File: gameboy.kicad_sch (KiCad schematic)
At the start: 17 parts, among them J1 FPC-05F-12PH20, J2 Conn_ST_STDC14, J3 Conn_01x02, U1 TP4056-42-ESOP8, U2 STM32F722RETx, Y1 26MHz

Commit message: start with power management
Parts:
- removed C3: C, symbol Device:C
- removed C4: 10uF, symbol Device:C
- removed D1, D2: LED, symbol Device:LED
- removed J3: Conn_01x02, Connector_JST:JST_PH_B2B-PH-K_1x02_P2.00mm_Vertical, symbol Connector_Generic:Conn_01x02
- removed R2: 2.2k, symbol Device:R
- removed R3, R4: 1k, symbol Device:R
- removed U1: TP4056-42-ESOP8, Package_SO:SOIC-8-1EP_3.9x4.9mm_P1.27mm_EP2.41x3.3mm_ThermalVias, symbol Battery_Management:TP4056-42-ESOP8
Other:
- added sheet Power (power.kicad_sch)
- note removed: "0.5C = half the battery capacity per hour 1000mAh => 500mA = I_{BAT} charge current R_{prog} = 1100 / I_{BAT} = 2.2k"
- note removed: "523450 LiPo 3.7V, 1000mAh"

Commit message: led driver backlight, not finished
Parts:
- added C8, C9: 1uF, Capacitor_SMD:C_0603_1608Metric, symbol Device:C
- added D5: D, symbol Device:D_Schottky
- added L2: 22uH, Inductor_SMD:L_KOHERelec_MDA7030, symbol Device:L
- added R11: 1.25R, Resistor_SMD:R_0603_1608Metric, symbol Device:R
- added U3: AP5724WG-7, SOT26_DIO:SOT26_DIO, symbol SOT26_DIO:AP5724WG-7
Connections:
- net GND: now also C8.2, C9.2, R11.2, U3.2 (GND)
- net LCD_BL_A: now also C9.1, D5.1 (K), U3.5 (OVP)
- net LCD_BL_K: now also R11.1, U3.3 (FB)
- new net: D5.2 (A), L2.2, U3.1 (SW)
- new net +BATT: C8.1, L2.1, U3.6 (VIN)
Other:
- note added: "2.8V"
- note added: "CHECK THIS"
- moved on the sheet: J1

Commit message: add buttons and connect lcd
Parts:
- removed C8, C9: 1uF, Capacitor_SMD:C_0603_1608Metric, symbol Device:C
- removed D5: D, symbol Device:D_Schottky
- removed J1: FPC-05F-12PH20, Connector_FFC-FPC:TE_1-1734839-2_1x12-1MP_P0.5mm_Horizontal, symbol Connector_Generic:Conn_01x12
- removed L2: 22uH, Inductor_SMD:L_KOHERelec_MDA7030, symbol Device:L
- removed R11: 1.25R, Resistor_SMD:R_0603_1608Metric, symbol Device:R
- removed U3: AP5724WG-7, SOT26_DIO:SOT26_DIO, symbol SOT26_DIO:AP5724WG-7
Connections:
- no-connect marks 2 -> 1
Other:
- added sheet Buttons (buttons.kicad_sch)
- added sheet LCD (lcd.kicad_sch)
- note removed: "2.8V"
- note removed: "CHECK THIS"
- note removed: "HS20HS072RX display"

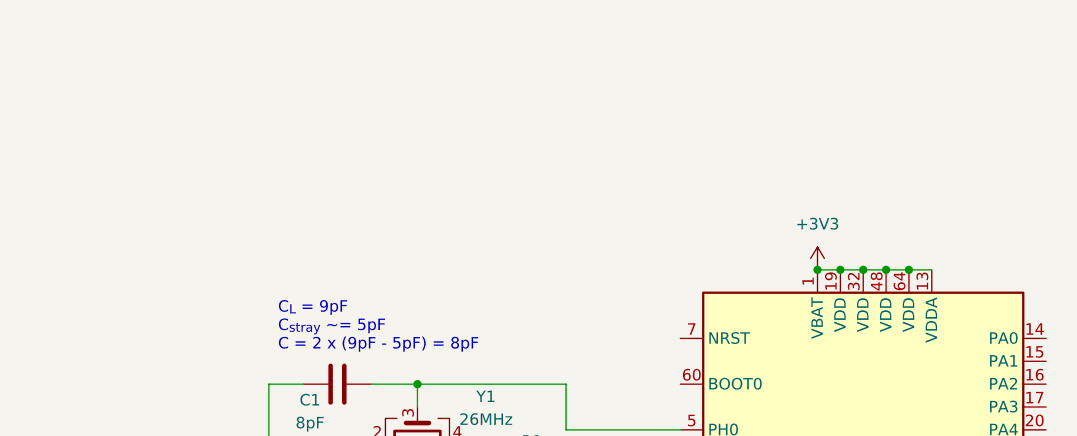
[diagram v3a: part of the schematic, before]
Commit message: button debouncing and VDD decoupling
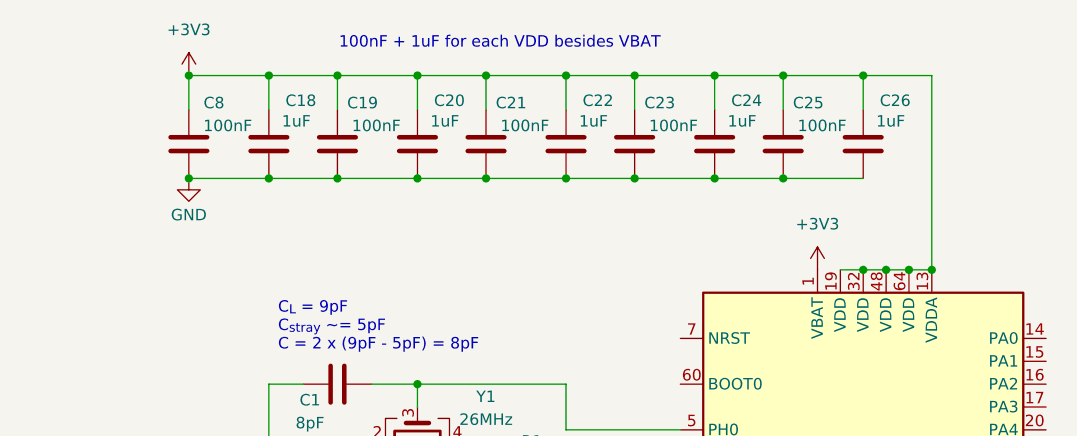
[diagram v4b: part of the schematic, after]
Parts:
- added C18, C20, C22, C24, C26: 1uF, Capacitor_SMD:C_0603_1608Metric, symbol Device:C
- added C19, C21, C23, C25, C8: 100nF, Capacitor_SMD:C_0603_1608Metric, symbol Device:C
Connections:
- net +3V3: now also C18.2, C19.2, C20.2, C21.2, C22.2, C23.2, C24.2, C25.2, C26.2, C8.2
- net GND: now also C18.1, C19.1, C20.1, C21.1, C22.1, C23.1, C24.1, C25.1, C26.1, C8.1
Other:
- note added: "100nF + 1uF for each VDD besides VBAT"

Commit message: remove backups, removed old chip
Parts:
- removed C1, C2: 8pF, Capacitor_SMD:C_0603_1608Metric, symbol Device:C
- removed C18, C20, C22, C24, C26: 1uF, Capacitor_SMD:C_0603_1608Metric, symbol Device:C
- removed C19, C21, C23, C25, C8: 100nF, Capacitor_SMD:C_0603_1608Metric, symbol Device:C
- removed C5: 2.2uF, symbol Device:C
- removed J2: Conn_ST_STDC14, Connector_PinHeader_1.27mm:PinHeader_2x07_P1.27mm_Vertical_SMD, symbol Connector:Conn_ST_STDC14
- removed R1: 0R, Resistor_SMD:R_0603_1608Metric, symbol Device:R
- removed U2: STM32F722RETx, Package_QFP:LQFP-64_10x10mm_P0.5mm, symbol MCU_ST_STM32F7:STM32F722RETx
- removed Y1: 26MHz, Crystal:Crystal_SMD_2016-4Pin_2.0x1.6mm, symbol Device:Crystal_GND24
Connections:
- no-connect marks 1 -> 0
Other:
- note removed: "100nF + 1uF for each VDD besides VBAT"
- note removed: "C_{L} = 9pF C_{stray} ~= 5pF C = 2 x (9pF - 5pF) = 8pF"
- note removed: "Programmer/Debugger"

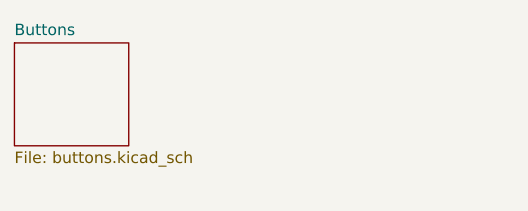
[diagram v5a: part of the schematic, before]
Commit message: add rp2350 mcu
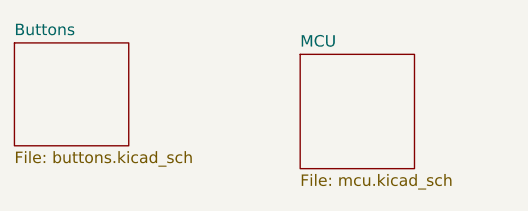
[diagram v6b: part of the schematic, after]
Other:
- added sheet MCU (mcu.kicad_sch)
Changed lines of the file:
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@@
+	)
+	(sheet
+		(at 124.46 170.18)
+		(size 12.7 12.7)
+		(exclude_from_sim no)
+		(in_bom yes)
+		(on_board yes)
+		(dnp no)
+		(fields_autoplaced yes)
+		(stroke
+			(width 0.1524)
+			(type solid)
+		)
+		(fill
+			(color 0 0 0 0.0000)
+		)
+		(property "Sheetname" "MCU"
+			(at 124.46 169.4684 0)
+			(effects
+				(font
+					(size 1.27 1.27)
+				)
+				(justify left bottom)
+			)
+		)
+		(property "Sheetfile" "mcu.kicad_sch"
+			(at 124.46 183.4646 0)
+			(effects
+				(font
+					(size 1.27 1.27)
+				)
+				(justify left top)
+			)
+		)
+		(instances
+			(project "gameboy"
+				(path "/f4643692-c319-40a7-82a2-3e775c0a417f"
+					(page "5")
+				)
+			)
+		)
 	)
 	(sheet

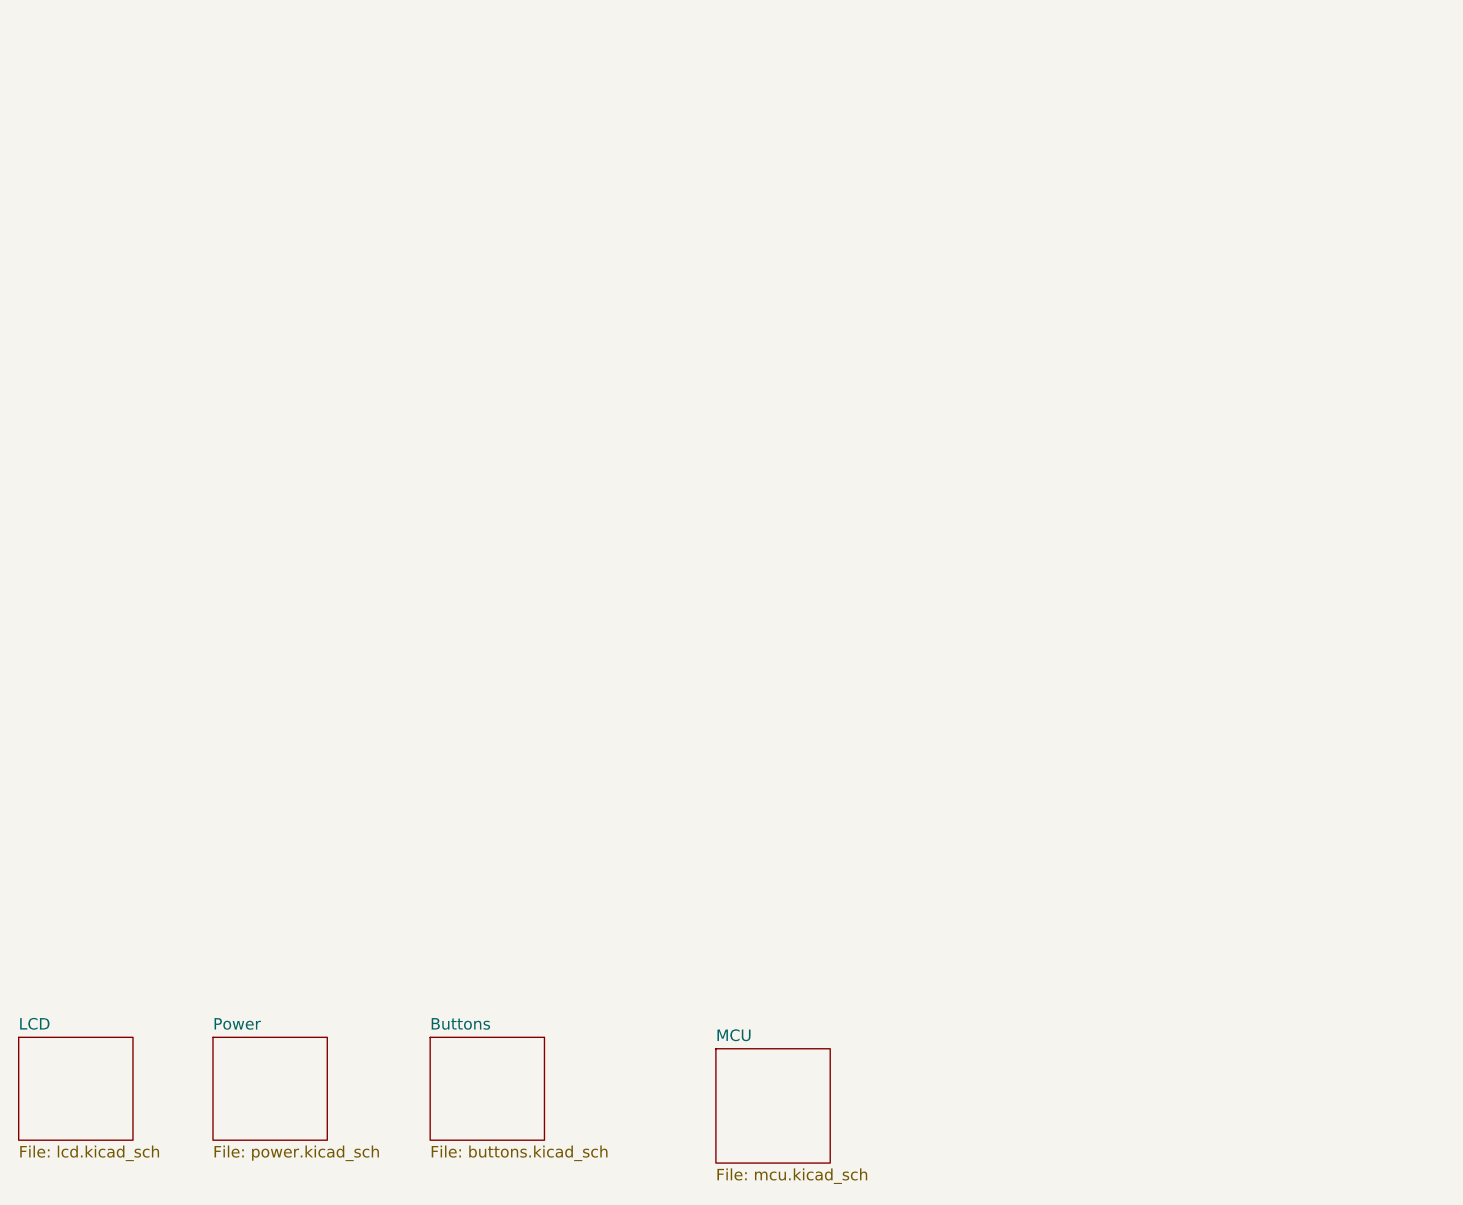
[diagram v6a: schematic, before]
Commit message: schematic functional and includes current test setup
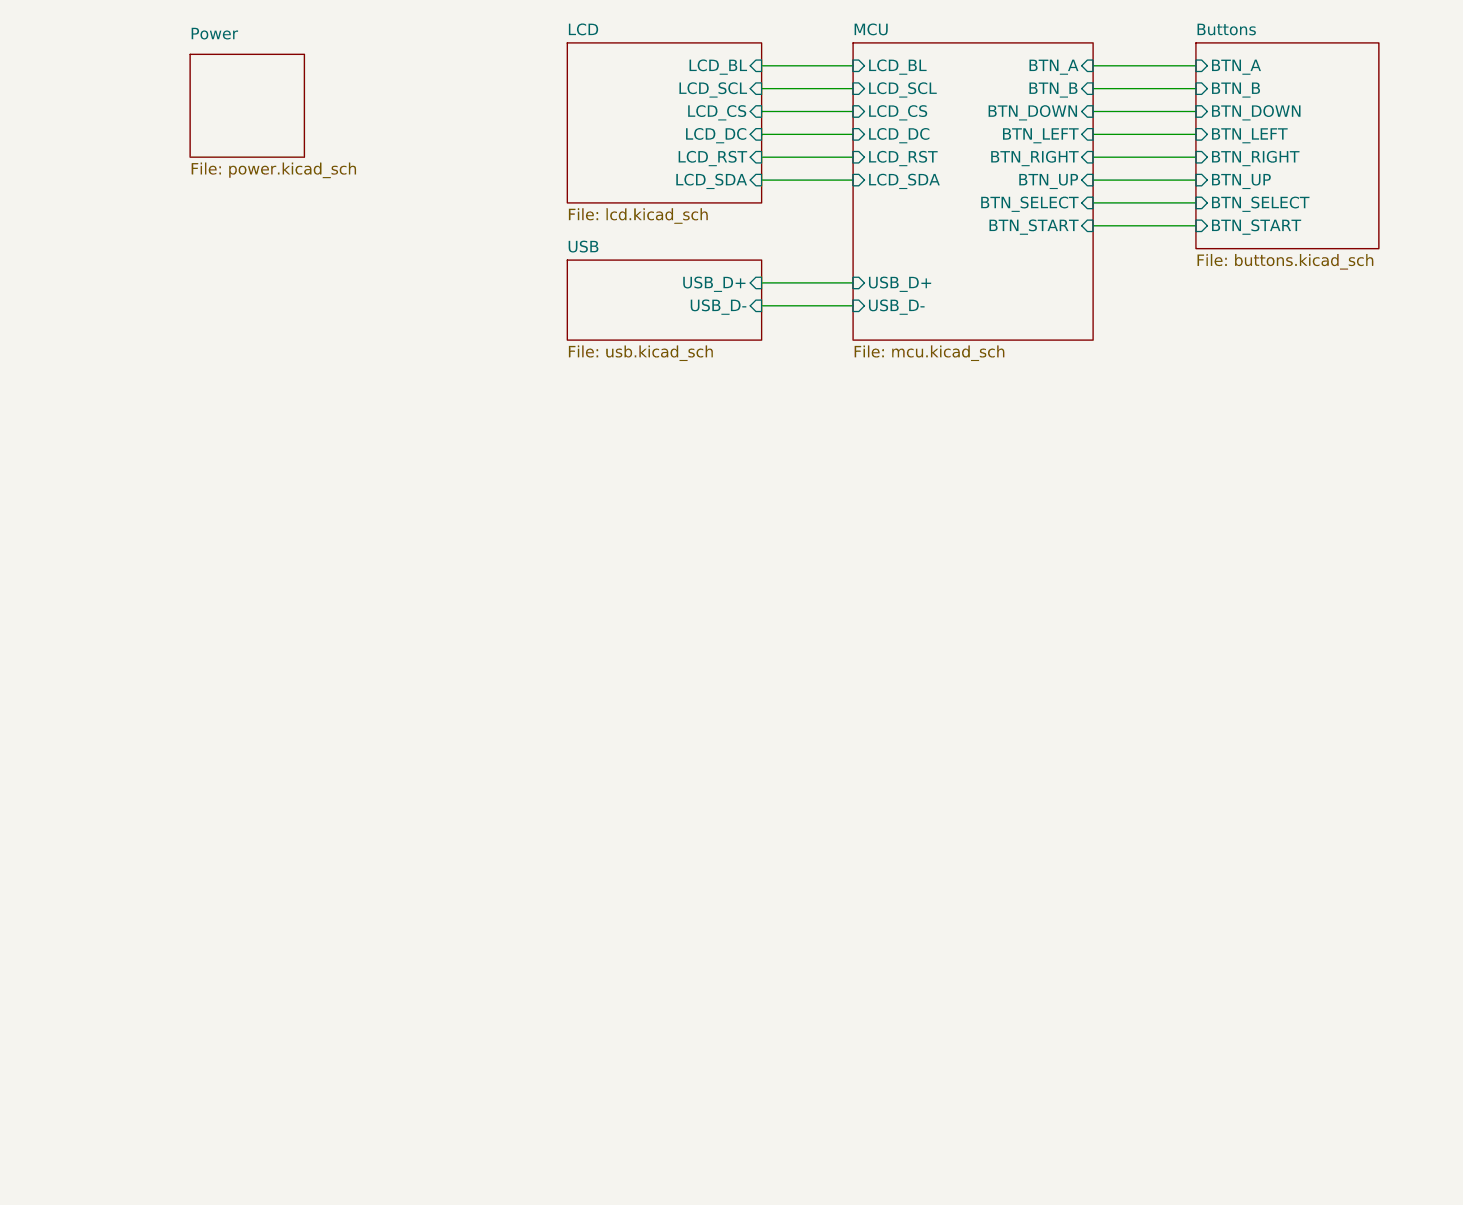
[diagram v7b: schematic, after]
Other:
- added sheet USB (usb.kicad_sch)
- sheet Buttons ports: added BTN_A, BTN_B, BTN_DOWN, BTN_LEFT, BTN_RIGHT, BTN_SELECT, BTN_START, BTN_UP; removed none
- sheet LCD ports: added LCD_BL, LCD_CS, LCD_DC, LCD_RST, LCD_SCL, LCD_SDA; removed none
- sheet MCU ports: added BTN_A, BTN_B, BTN_DOWN, BTN_LEFT, BTN_RIGHT, BTN_SELECT, BTN_START, BTN_UP, LCD_BL, LCD_CS, LCD_DC, LCD_RST, LCD_SCL, LCD_SDA, USB_D+, USB_D-; removed none

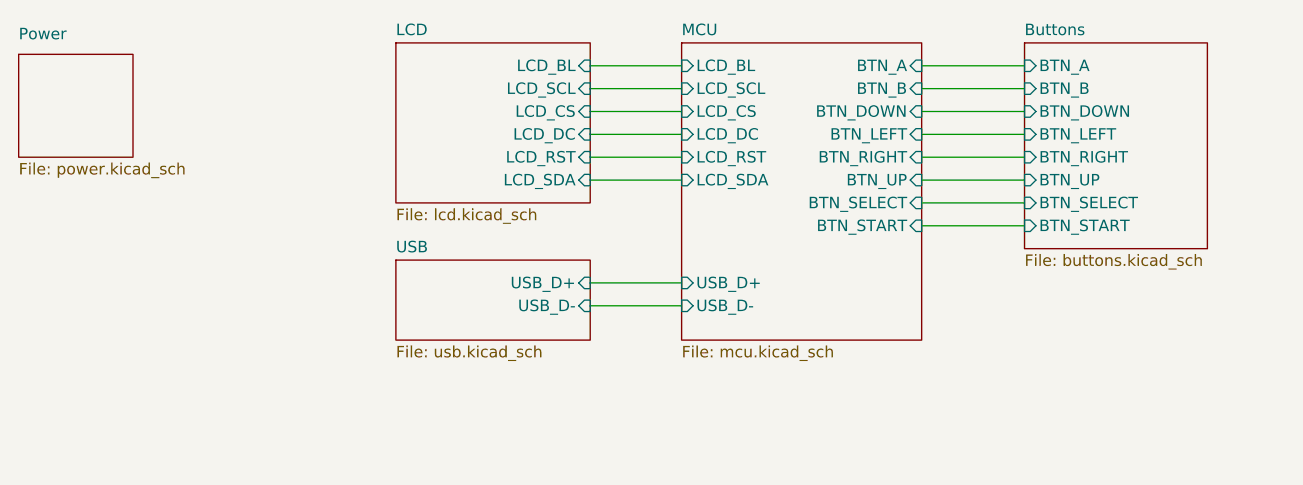
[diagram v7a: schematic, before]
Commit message: add audio amp
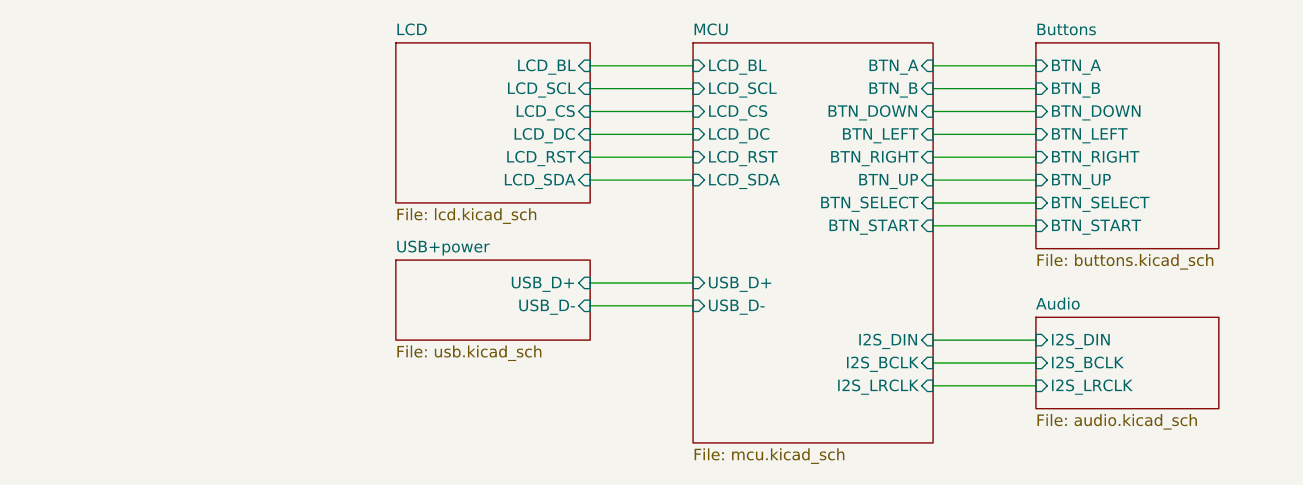
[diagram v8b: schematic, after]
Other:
- sheet USB renamed USB+power
- removed sheet Power
- added sheet Audio (audio.kicad_sch)
- sheet MCU ports: added I2S_BCLK, I2S_DIN, I2S_LRCLK; removed none
